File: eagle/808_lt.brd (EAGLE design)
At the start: 100.8 x 80.8 mm, 58 parts, among them IC1 TL071P, IC2 TL072P, Q1 2N3904, Q2 2N3906, Q3 2N3904, SW8 MSS42_SW_4PDT

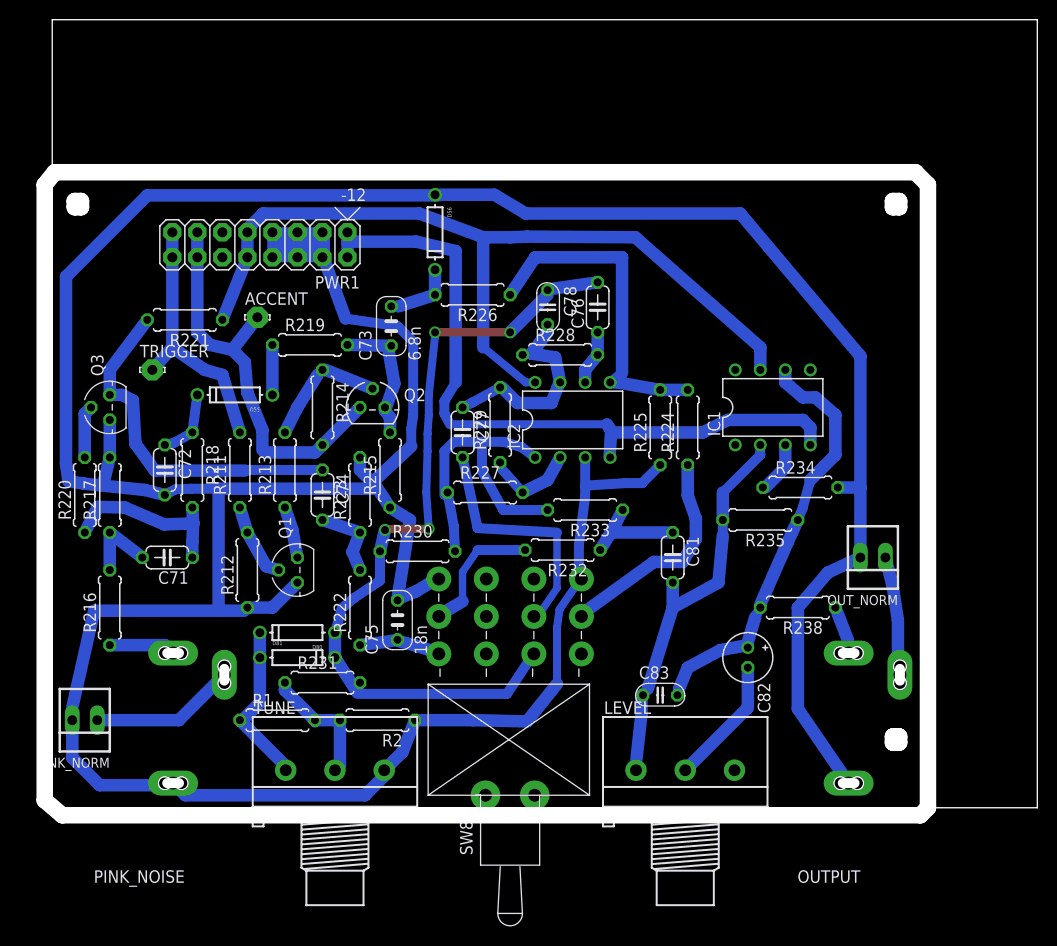
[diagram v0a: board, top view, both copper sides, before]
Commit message: corrected 4pdt toggle body size
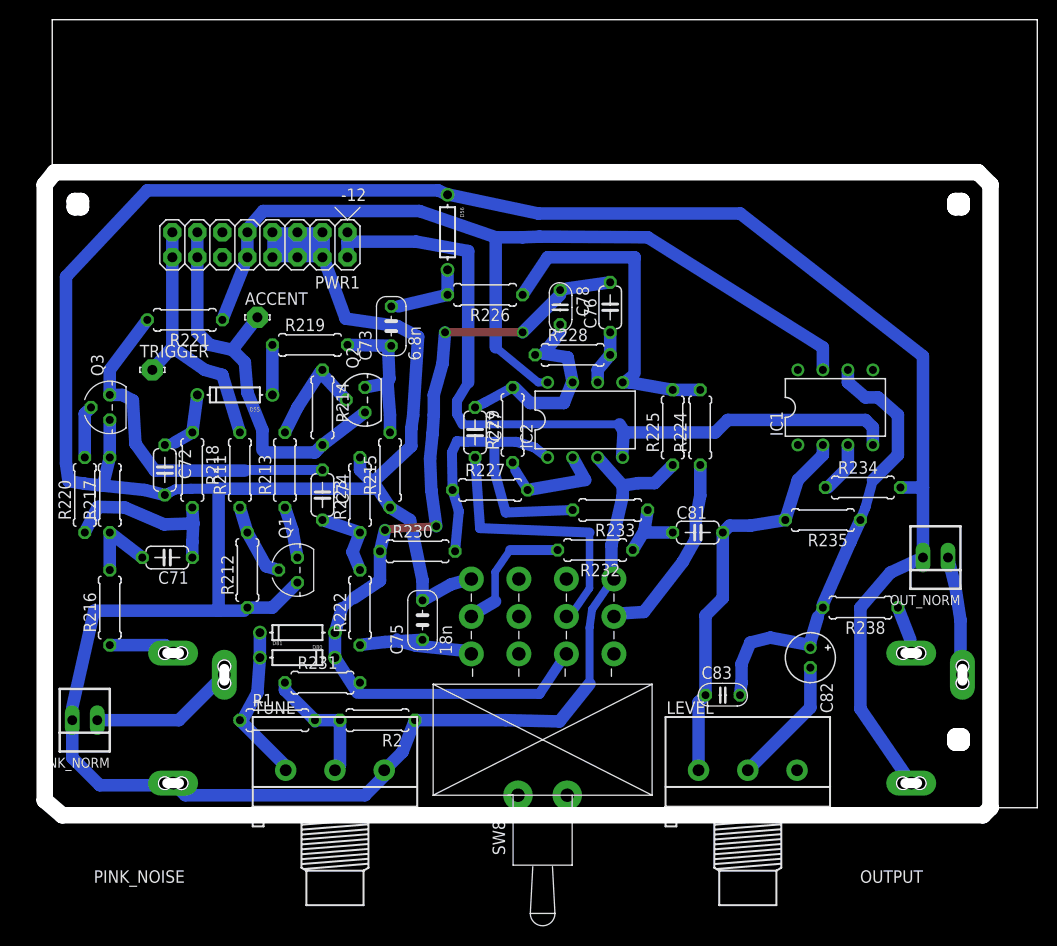
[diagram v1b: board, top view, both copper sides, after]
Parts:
- SW8: value MSS42_SW_4PDT -> 808_LT_MSS42_SW_4PDT; device 808_lt:MSS42_SW_SLIDE -> 808_lt:808_LT_MSS42_SW_SLIDE
- moved C82 6.35 mm to (77.0, 15.2)
- moved OUT_NORM 6.35 mm to (89.7, 25.4)
- moved R234 6.35 mm to (82.3, 32.5)
- moved R238 6.35 mm to (82.0, 20.3)
- moved C83 6.35 mm to (68.1, 11.4)
- moved IC1 6.35 mm to (79.5, 40.6)
- moved LEVEL 6.35 mm to (70.6, 3.81)
- moved OUTPUT 6.35 mm to (92.2, 0.00)
- moved R235 6.35 mm to (78.2, 29.2)
- moved C81 3.59 mm to (65.5, 27.9), turned to 0 degrees
- moved R232 3.30 mm to (55.1, 26.2)
- moved SW8 3.30 mm to (49.8, 1.27)
- moved R233 2.54 mm to (56.6, 30.2)
- moved C75 2.54 mm to (37.6, 19.1)
- moved C76 1.27 mm to (56.6, 50.8)
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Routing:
- net N$264: track 8.65 -> 16.9 mm
- net GND: track 405.1 -> 412.4 mm
- net -15V: track 73.8 -> 80.4 mm
- net +15V: track 87.1 -> 92.6 mm
- net N$251: track 84.0 -> 88.2 mm
- net N$259: track 10.9 -> 7.38 mm
- net N$271: track 25.5 -> 28.4 mm
- net N$111: track 22.5 -> 19.9 mm
- net N$256: track 9.32 -> 11.7 mm
- net N$257: track 32.9 -> 35.2 mm
- net N$241: track 13.5 -> 11.3 mm
- net N$262: track 43.2 -> 45.3 mm
- net N$247: track 14.1 -> 15.8 mm
- net N$250: track 7.17 -> 8.39 mm
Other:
- outline, holes or cut-outs redrawn
